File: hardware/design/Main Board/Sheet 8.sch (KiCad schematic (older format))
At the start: 8 parts

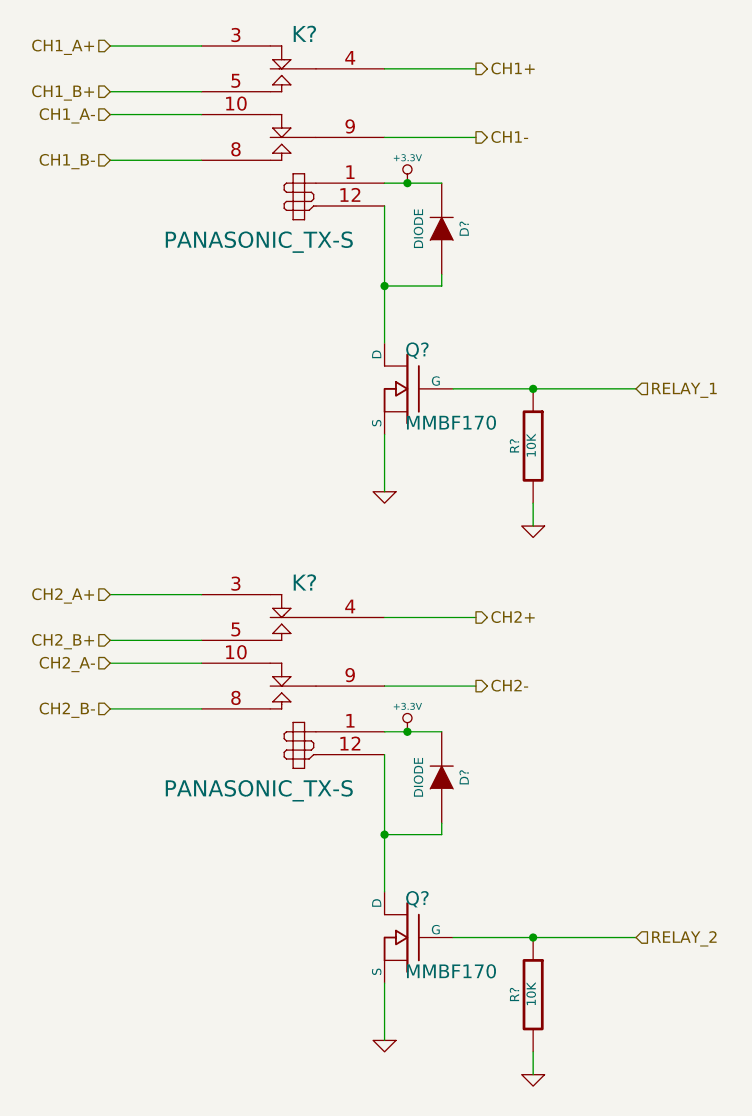
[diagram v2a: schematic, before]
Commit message: Version 1.0.082514.2134
Initial partial PCB layout.
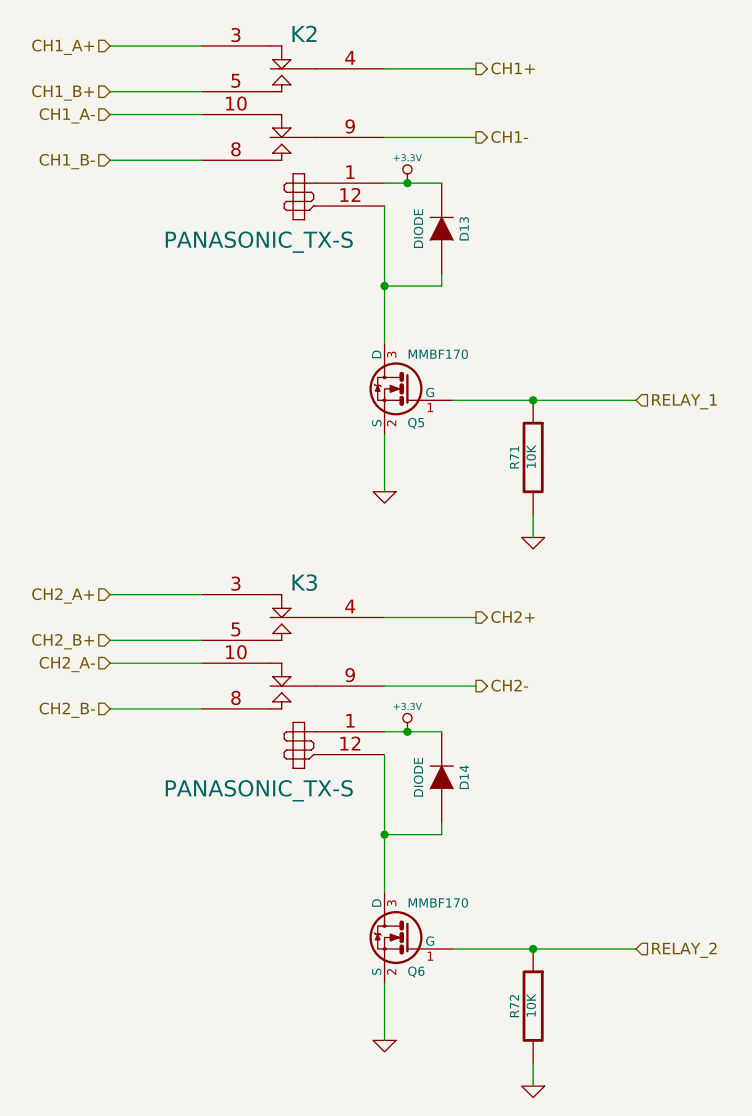
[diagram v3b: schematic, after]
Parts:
- removed Q? (x2): MMBF170, ~, symbol MOSFET_N
- added Q5, Q6: MMBF170, SOT-23, symbol BSS138
- gave numbers to parts that had none: 6
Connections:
- net GND: now also Q5.2 (S), Q6.2 (S)
- net RELAY_1: now also Q5.1 (G)
- net RELAY_2: now also Q6.1 (G)
- net at D14.1 (A), K3.12 (-): now also Q6.3 (D)
- net at D13.1 (A), K2.12 (-): now also Q5.3 (D)
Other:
- moved on the sheet: R71, R72
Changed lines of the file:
@@
 Sheet 9 9
 Title "Hybrid Audio Dynamics Processor"
-Date "15 may 2014"
+Date "26 aug 2014"
 Rev "1.0"
 Comp "P14345"
@@
 $EndDescr
 $Comp
-L PANASONIC_TX-S K?
+L PANASONIC_TX-S K3
 U 1 1 536F9B0D
 P 5550 4800
-F 0 "K?" H 5500 5200 70  0000 C CNN
+F 0 "K3" H 5500 5200 70  0000 C CNN
 F 1 "PANASONIC_TX-S" H 5700 4300 70  0000 C CNN
 F 2 "~" H 5550 4800 60  0000 C CNN
@@
 $EndComp
 $Comp
-L +3.3V #PWR?
+L +3.3V #PWR0117
 U 1 1 536F9B3D
 P 6050 5050
-F 0 "#PWR?" H 6050 5010 30  0001 C CNN
+F 0 "#PWR0117" H 6050 5010 30  0001 C CNN
 F 1 "+3.3V" H 6050 5160 30  0000 C CNN
 F 2 "" H 6050 5050 60  0000 C CNN
@@
 Wire Wire Line
 	6200 5050 5950 5050
-$Comp
-L MOSFET_N Q?
-U 1 1 536F9B52
-P 6050 5950
-F 0 "Q?" H 6060 6120 60  0000 R CNN
-F 1 "MMBF170" H 6060 5800 60  0000 R CNN
-F 2 "~" H 6050 5950 60  0000 C CNN
-F 3 "~" H 6050 5950 60  0000 C CNN
-	1    6050 5950
-	-1   0    0    -1
-$EndComp
 Wire Wire Line
 	5950 5150 5950 5750
 $Comp
-L R R?
+L R R72
 U 1 1 536F9B80
-P 6600 6200
-F 0 "R?" V 6680 6200 40  0000 C CNN
-F 1 "10K" V 6607 6201 40  0000 C CNN
-F 2 "~" V 6530 6200 30  0000 C CNN
-F 3 "~" H 6600 6200 30  0000 C CNN
-	1    6600 6200
-	-1   0    0    -1
-$EndComp
-$Comp
-L DIODE D?
+P 6600 6250
+F 0 "R72" V 6680 6250 40  0000 C CNN
+F 1 "10K" V 6607 6251 40  0000 C CNN
+F 2 "~" V 6530 6250 30  0000 C CNN
+F 3 "~" H 6600 6250 30  0000 C CNN
+	1    6600 6250
+	-1   0    0    -1
+$EndComp
+$Comp
+L DIODE D14
 U 1 1 536F9B88
 P 6200 5250
-F 0 "D?" H 6200 5350 40  0000 C CNN
+F 0 "D14" H 6200 5350 40  0000 C CNN
 F 1 "DIODE" H 6200 5150 40  0000 C CNN
 F 2 "~" H 6200 5250 60  0000 C CNN
@@
 Connection ~ 5950 5500
 $Comp
-L GND #PWR?
+L GND #PWR0118
 U 1 1 536F9BDD
 P 5950 6400
-F 0 "#PWR?" H 5950 6400 30  0001 C CNN
+F 0 "#PWR0118" H 5950 6400 30  0001 C CNN
 F 1 "GND" H 5950 6330 30  0001 C CNN
 F 2 "" H 5950 6400 60  0000 C CNN
@@
 	5950 6150 5950 6400
 Wire Wire Line
-	7050 5950 6250 5950
-$Comp
-L GND #PWR?
+	7050 6000 6250 6000
+$Comp
+L GND #PWR0119
 U 1 1 536F9C03
-P 6600 6550
-F 0 "#PWR?" H 6600 6550 30  0001 C CNN
-F 1 "GND" H 6600 6480 30  0001 C CNN
-F 2 "" H 6600 6550 60  0000 C CNN
-F 3 "" H 6600 6550 60  0000 C CNN
-	1    6600 6550
-	-1   0    0    -1
-$EndComp
-Wire Wire Line
-	6600 6550 6600 6450
-Connection ~ 6600 5950
+P 6600 6600
+F 0 "#PWR0119" H 6600 6600 30  0001 C CNN
+F 1 "GND" H 6600 6530 30  0001 C CNN
+F 2 "" H 6600 6600 60  0000 C CNN
+F 3 "" H 6600 6600 60  0000 C CNN
+	1    6600 6600
+	-1   0    0    -1
+$EndComp
+Wire Wire Line
+	6600 6600 6600 6500
+Connection ~ 6600 6000
 Wire Wire Line
 	5950 4850 6350 4850
@@
 	4750 4950 5150 4950
 $Comp
-L PANASONIC_TX-S K?
+L PANASONIC_TX-S K2
 U 1 1 536F9E96
 P 5550 2400
-F 0 "K?" H 5500 2800 70  0000 C CNN
+F 0 "K2" H 5500 2800 70  0000 C CNN
 F 1 "PANASONIC_TX-S" H 5700 1900 70  0000 C CNN
 F 2 "~" H 5550 2400 60  0000 C CNN
@@
 $EndComp
 $Comp
-L +3.3V #PWR?
+L +3.3V #PWR0120
 U 1 1 536F9E9C
 P 6050 2650
-F 0 "#PWR?" H 6050 2610 30  0001 C CNN
+F 0 "#PWR0120" H 6050 2610 30  0001 C CNN
 F 1 "+3.3V" H 6050 2760 30  0000 C CNN
 F 2 "" H 6050 2650 60  0000 C CNN
@@
 Wire Wire Line
 	6200 2650 5950 2650
-$Comp
-L MOSFET_N Q?
-U 1 1 536F9EA3
-P 6050 3550
-F 0 "Q?" H 6060 3720 60  0000 R CNN
-F 1 "MMBF170" H 6060 3400 60  0000 R CNN
-F 2 "~" H 6050 3550 60  0000 C CNN
-F 3 "~" H 6050 3550 60  0000 C CNN
-	1    6050 3550
-	-1   0    0    -1
-$EndComp
 Wire Wire Line
 	5950 2750 5950 3350
 $Comp
-L R R?
+L R R71
 U 1 1 536F9EAA
-P 6600 3800
-F 0 "R?" V 6680 3800 40  0000 C CNN
-F 1 "10K" V 6607 3801 40  0000 C CNN
-F 2 "~" V 6530 3800 30  0000 C CNN
-F 3 "~" H 6600 3800 30  0000 C CNN
-	1    6600 3800
-	-1   0    0    -1
-$EndComp
-$Comp
-L DIODE D?
+P 6600 3850
+F 0 "R71" V 6680 3850 40  0000 C CNN
+F 1 "10K" V 6607 3851 40  0000 C CNN
+F 2 "~" V 6530 3850 30  0000 C CNN
+F 3 "~" H 6600 3850 30  0000 C CNN
+	1    6600 3850
+	-1   0    0    -1
+$EndComp
+$Comp
+L DIODE D13
 U 1 1 536F9EB0
 P 6200 2850
-F 0 "D?" H 6200 2950 40  0000 C CNN
+F 0 "D13" H 6200 2950 40  0000 C CNN
 F 1 "DIODE" H 6200 2750 40  0000 C CNN
 F 2 "~" H 6200 2850 60  0000 C CNN
@@
 Connection ~ 5950 3100
 $Comp
-L GND #PWR?
+L GND #PWR0121
 U 1 1 536F9EBA
 P 5950 4000
-F 0 "#PWR?" H 5950 4000 30  0001 C CNN
+F 0 "#PWR0121" H 5950 4000 30  0001 C CNN
 F 1 "GND" H 5950 3930 30  0001 C CNN
 F 2 "" H 5950 4000 60  0000 C CNN
@@
 	5950 3750 5950 4000
 Wire Wire Line
-	7050 3550 6250 3550
-$Comp
-L GND #PWR?
+	7050 3600 6250 3600
+$Comp
+L GND #PWR0122
 U 1 1 536F9EC2
-P 6600 4150
-F 0 "#PWR?" H 6600 4150 30  0001 C CNN
-F 1 "GND" H 6600 4080 30  0001 C CNN
-F 2 "" H 6600 4150 60  0000 C CNN
-F 3 "" H 6600 4150 60  0000 C CNN
-	1    6600 4150
-	-1   0    0    -1
-$EndComp
-Wire Wire Line
-	6600 4150 6600 4050
-Connection ~ 6600 3550
+P 6600 4200
+F 0 "#PWR0122" H 6600 4200 30  0001 C CNN
+F 1 "GND" H 6600 4130 30  0001 C CNN
+F 2 "" H 6600 4200 60  0000 C CNN
+F 3 "" H 6600 4200 60  0000 C CNN
+	1    6600 4200
+	-1   0    0    -1
+$EndComp
+Wire Wire Line
+	6600 4200 6600 4100
+Connection ~ 6600 3600
 Wire Wire Line
 	5950 2450 6350 2450
@@
 Wire Wire Line
 	4750 2550 5150 2550
-Text HLabel 7050 3550 2    50   Input ~ 0
+Text HLabel 7050 3600 2    50   Input ~ 0
 RELAY_1
-Text HLabel 7050 5950 2    50   Input ~ 0
+Text HLabel 7050 6000 2    50   Input ~ 0
 RELAY_2
 Text HLabel 4750 2050 0    50   Input ~ 0
@@
 Text HLabel 6350 4850 2    50   Output ~ 0
 CH2-
+$Comp
+L BSS138 Q6
+U 1 1 53F10CC1
+P 6050 5950
+F 0 "Q6" H 6050 5801 40  0000 R CNN
+F 1 "MMBF170" H 6050 6100 40  0000 R CNN
+F 2 "SOT-23" H 5920 6052 29  0001 C CNN
+F 3 "~" H 6050 5950 60  0000 C CNN
+	1    6050 5950
+	-1   0    0    -1
+$EndComp
+$Comp
+L BSS138 Q5
+U 1 1 53F10CF4
+P 6050 3550
+F 0 "Q5" H 6050 3401 40  0000 R CNN
+F 1 "MMBF170" H 6050 3700 40  0000 R CNN
+F 2 "SOT-23" H 5920 3652 29  0001 C CNN
+F 3 "~" H 6050 3550 60  0000 C CNN
+	1    6050 3550
+	-1   0    0    -1
+$EndComp
 $EndSCHEMATC
